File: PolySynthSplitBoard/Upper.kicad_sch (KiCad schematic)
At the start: 3 parts, among them J801 A_UPPER, J802 B_UPPER, J803 C_UPPER

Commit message: lower board
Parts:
- added J804: D_UPPER, Connector_PinSocket_2.54mm:PinSocket_1x03_P2.54mm_Vertical, symbol Connector:Conn_01x03_Pin
- added RV801: 100kA, Potentiometer_THT:Potentiometer_Bourns_PTV09A-1_Single_Vertical, symbol Device:R_Potentiometer_US
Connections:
- net GNDA: now also J804.1 (Pin_1), RV801.3
- new net VOL_A_U: J804.2 (Pin_2), RV801.1
- new net VOL_W_U: J804.3 (Pin_3), RV801.2
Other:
- note added: "Master volume control"
- moved on the sheet: J801, J802, J803

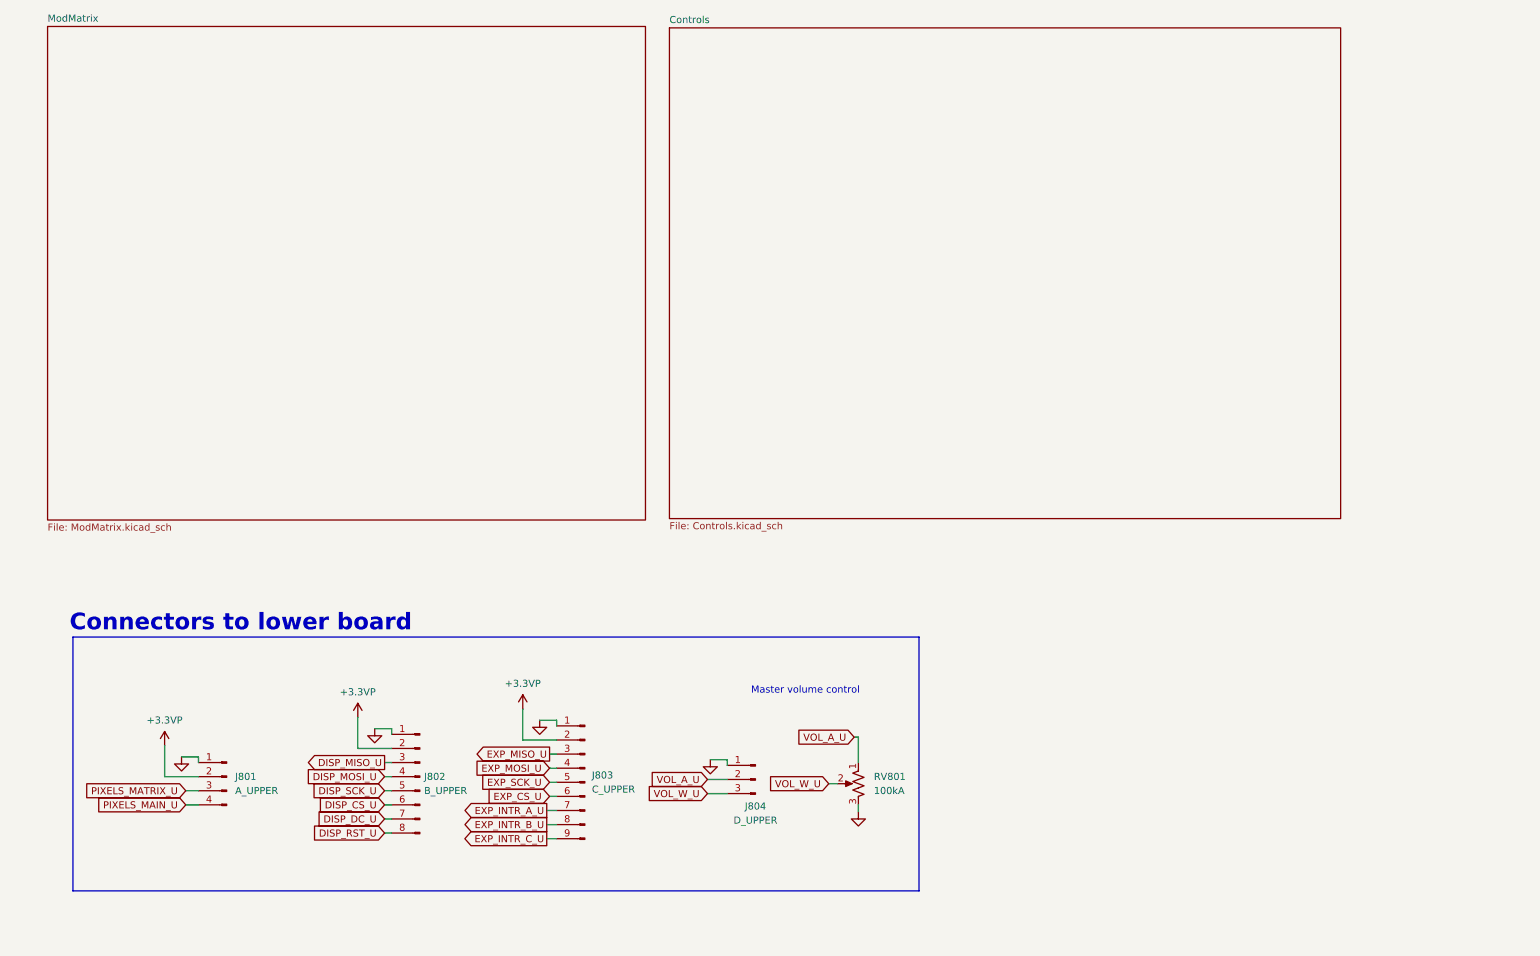
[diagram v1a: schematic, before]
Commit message: switching to 20p mezzanine connectors
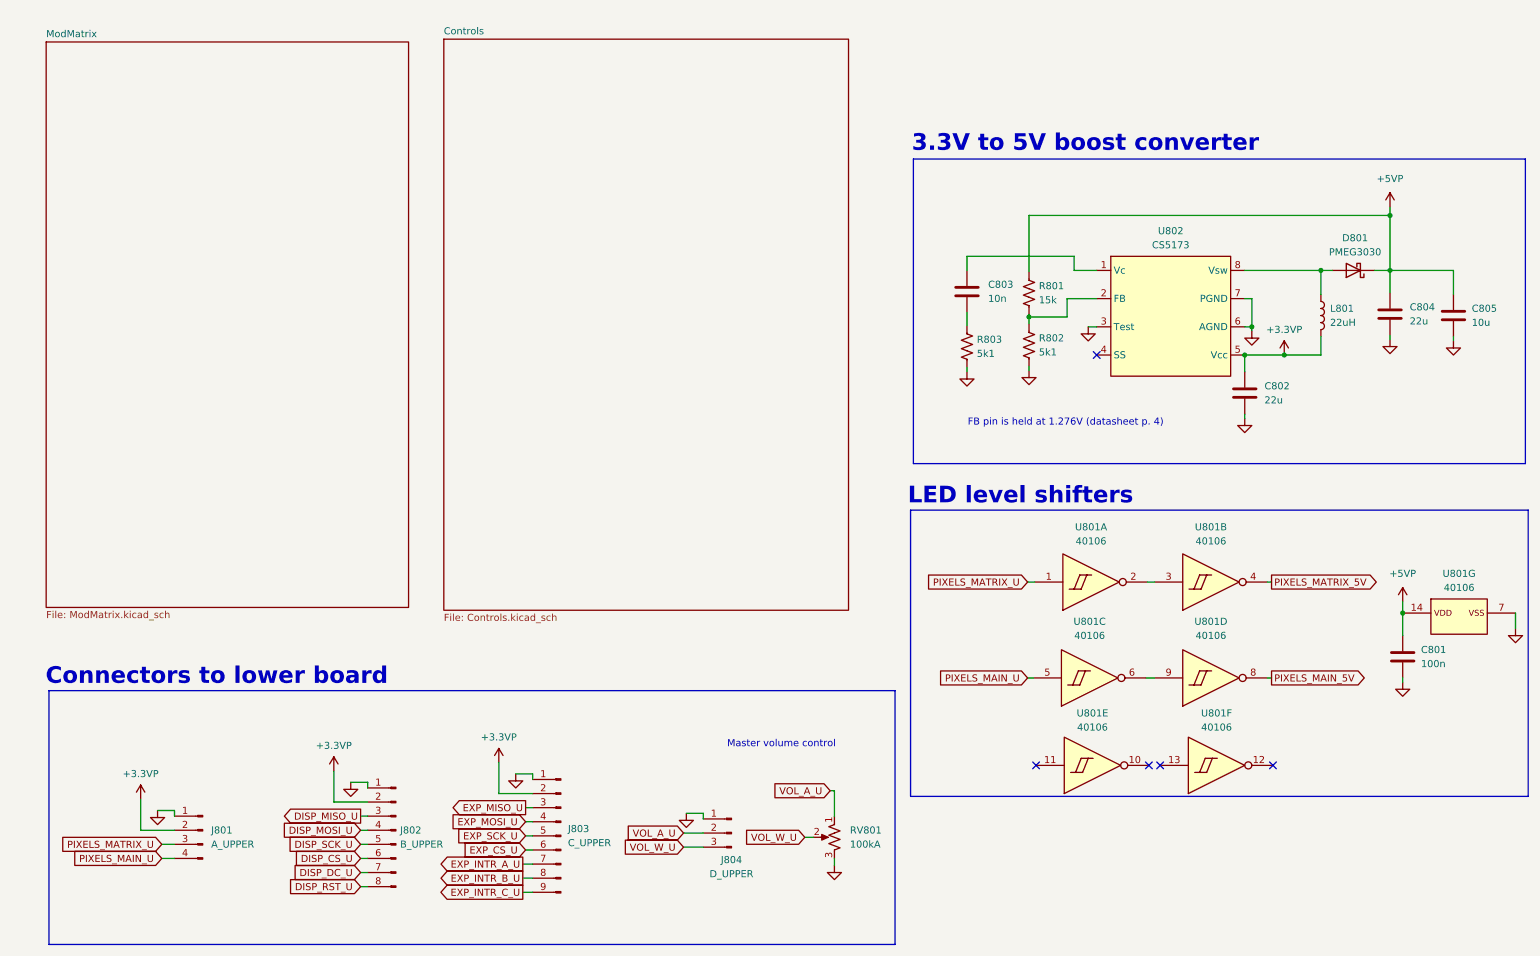
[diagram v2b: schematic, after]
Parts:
- added C801: 100n, Capacitor_SMD:C_0805_2012Metric, symbol Device:C
- added C802, C804: 22u, Capacitor_SMD:C_0805_2012Metric, symbol Device:C
- added C803: 10n, Capacitor_SMD:C_0805_2012Metric, symbol Device:C
- added C805: 10u, Capacitor_SMD:C_0805_2012Metric, symbol Device:C
- added D801: PMEG3030, Diode_SMD:D_SOD-123, symbol Device:D_Schottky
- added L801: 22uH, Inductor_SMD:L_Changjiang_FNR4010S, symbol Device:L
- added R801: 15k, Resistor_SMD:R_0805_2012Metric, symbol Device:R_US
- added R802, R803: 5k1, Resistor_SMD:R_0805_2012Metric, symbol Device:R_US
- added U801: CD40106BPWR, Package_SO:SOIC-14-16_3.9x9.9mm_P1.27mm, symbol PCM_4ms_IC:CD40106BPWR
- added U802: CS5173, Package_SO:SOIC-8_3.9x4.9mm_P1.27mm, symbol cs5173:CS5173
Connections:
- net +3.3VP: now also C802.1, L801.2, U802.5 (Vcc)
- net GNDA: now also C801.2, C802.2, C804.2, C805.2, R802.2, R803.2, U801.7 (VSS), U802.3 (Test), U802.6 (AGND), U802.7 (PGND)
- net PIXELS_MAIN_U: now also U801.5 (I)
- net PIXELS_MATRIX_U: now also U801.1 (I)
- new net: D801.2 (A), L801.1, U802.8 (Vsw)
- new net: C803.1, U802.1 (Vc)
- new net: R801.2, R802.1, U802.2 (FB)
- new net: U801.2 (O), U801.3 (I)
- new net: U801.6 (O), U801.9 (I)
- new net: C803.2, R803.1
- new net +5VP: C801.1, C804.1, C805.1, D801.1 (K), R801.1, U801.14 (VDD)
- new net PIXELS_MAIN_5V: U801.8 (O)
- new net PIXELS_MATRIX_5V: U801.4 (O)
- no-connect marks 0 -> 5
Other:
- note added: "3.3V to 5V boost converter"
- note added: "FB pin is held at 1.276V (datasheet p. 4)"
- note added: "LED level shifters"
- moved on the sheet: J801, J802, J803, J804, RV801

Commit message: motherboard rev2 passing DRC
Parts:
- removed U801: CD40106BPWR, Package_SO:SOIC-14-16_3.9x9.9mm_P1.27mm, symbol PCM_4ms_IC:CD40106BPWR
- added C806: 100n, Capacitor_SMD:C_0805_2012Metric, symbol Device:C
- added U801: 40106, Package_SO:SOIC-14_3.9x8.7mm_P1.27mm, symbol 4xxx:40106
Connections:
- net +5VP: now also C806.1, U801.14 (VDD)
- net GNDA: now also C806.2, U801.7 (VSS)
- net PIXELS_MAIN_5V: now also U801.8
- net PIXELS_MAIN_U: now also U801.11
- net PIXELS_MATRIX_5V: now also U801.4
- net PIXELS_MATRIX_U: now also U801.1
- new net: U801.2, U801.3
- new net: U801.10, U801.9
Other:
- moved on the sheet: C802, C803, C804, C805, D801, L801, R801, R802, R803, U802
